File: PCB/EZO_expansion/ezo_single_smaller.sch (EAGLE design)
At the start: 7 parts

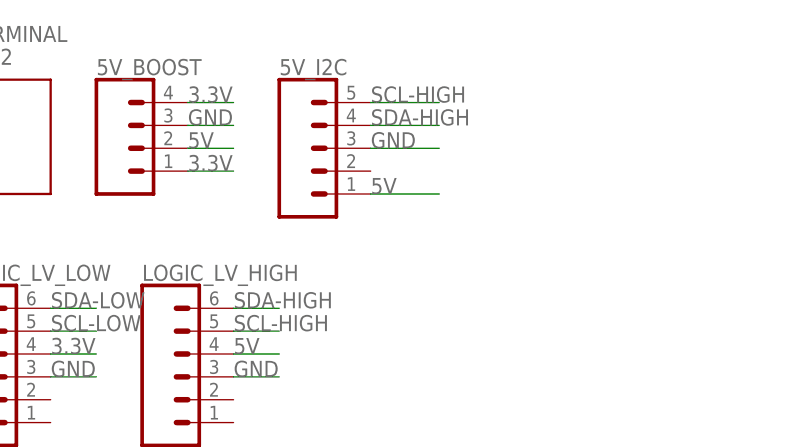
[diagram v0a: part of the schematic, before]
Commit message: Tied the OFF Pin on the EZO Isolated Carrier board to high, hopefully fixing our issues of fried DO circuits
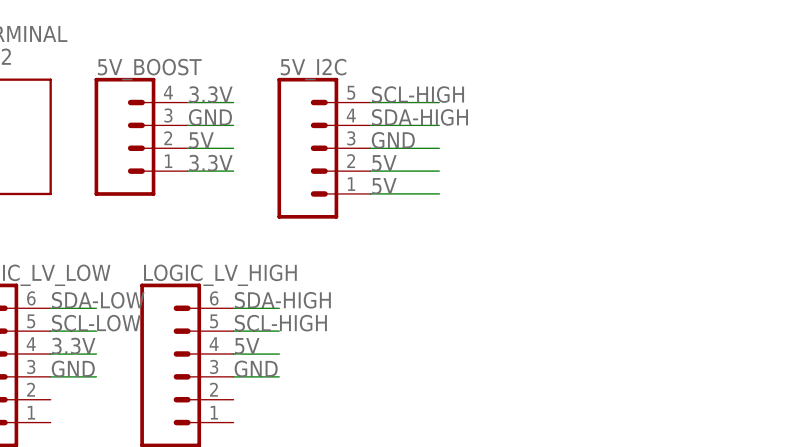
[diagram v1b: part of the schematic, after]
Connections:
- net 5V: now also 5V_I2C.2
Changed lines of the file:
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@@
 <label x="71.12" y="50.8" size="1.778" layer="95"/>
+</segment>
+<segment>
+<pinref part="5V_I2C" gate="J1" pin="2"/>
+<wire x1="71.12" y1="53.34" x2="78.74" y2="53.34" width="0.1524" layer="91"/>
+<label x="71.12" y="53.34" size="1.778" layer="95"/>
 </segment>
 </net>
